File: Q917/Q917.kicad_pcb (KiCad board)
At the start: 2 copper layers, 43.2 x 17.8 mm, 6 parts, among them J1 Analog, J2 Digital

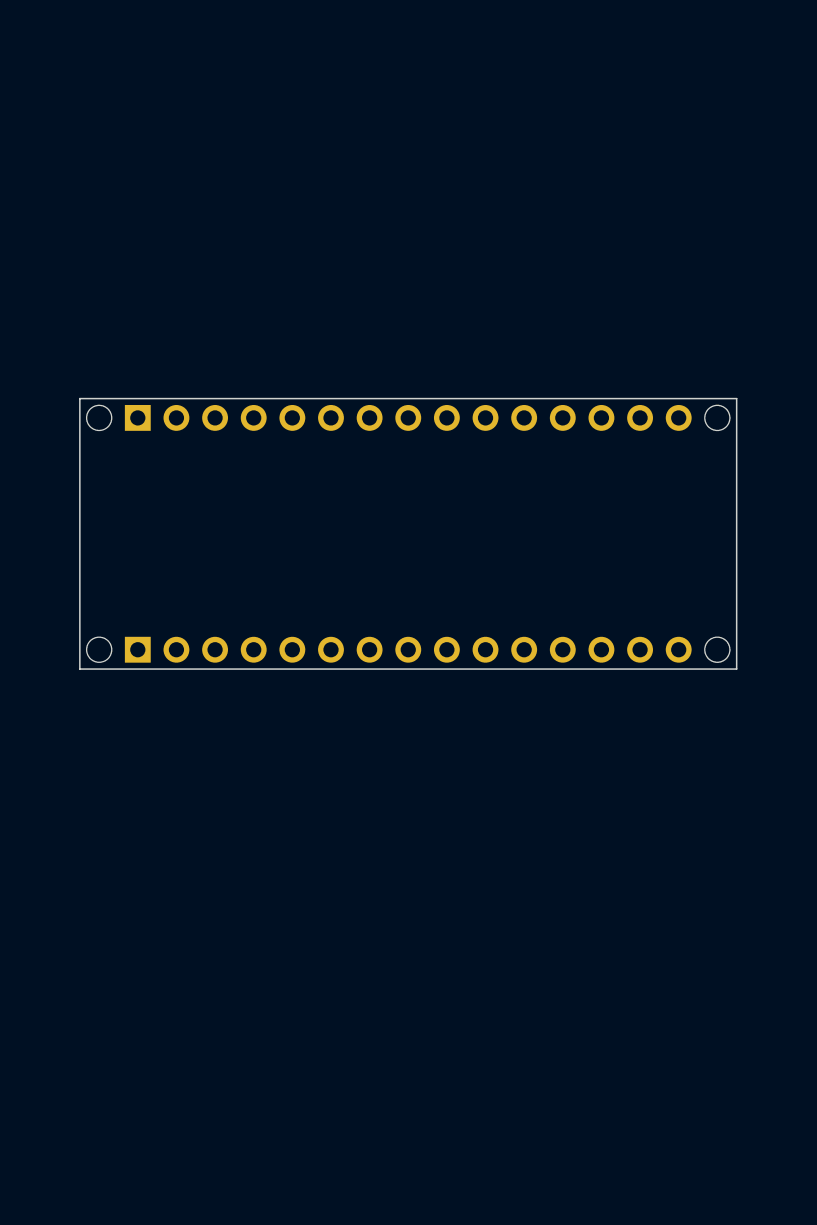
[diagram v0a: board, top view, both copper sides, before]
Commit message: sche: PCB配線開始
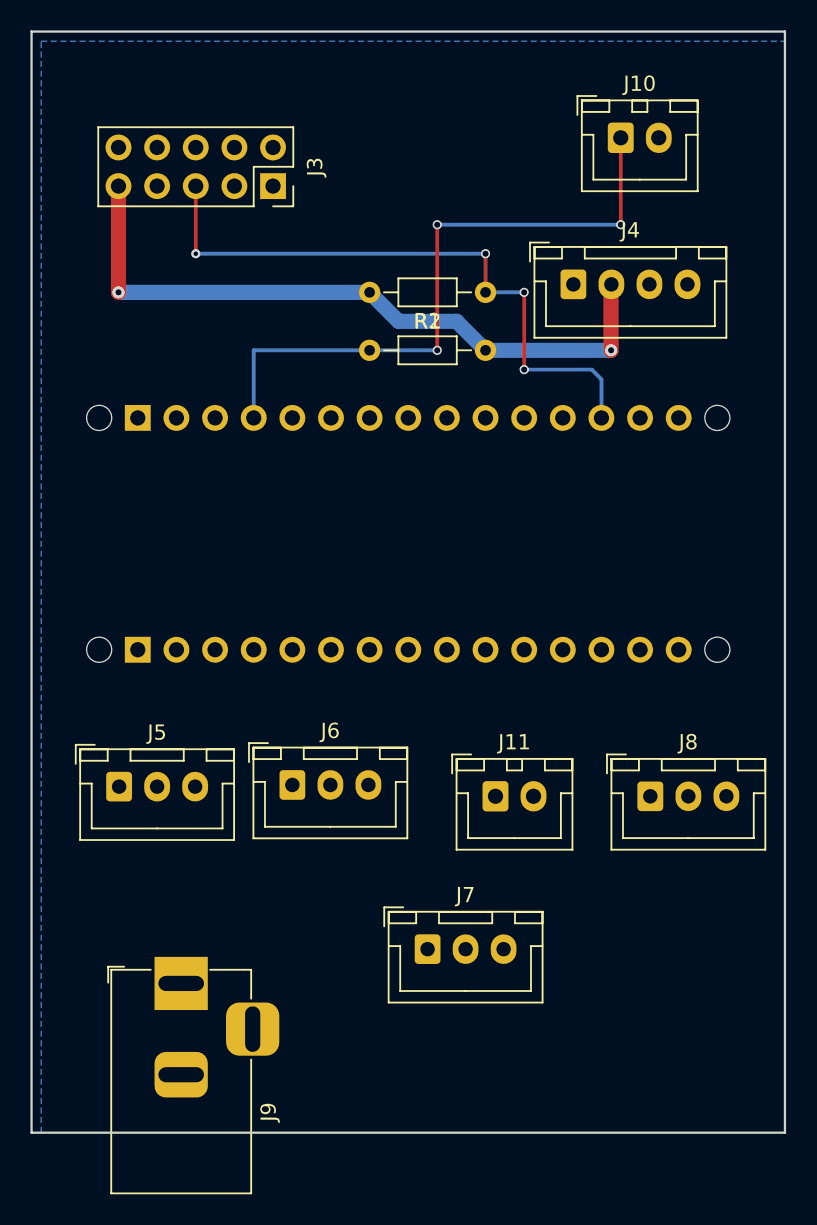
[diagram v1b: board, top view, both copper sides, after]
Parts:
- added J10: SELE, Connector_JST:JST_XH_B2B-XH-A_1x02_P2.50mm_Vertical, F.Cu at (135.6, 65.1)
- added J11: RESET, Connector_JST:JST_XH_B2B-XH-A_1x02_P2.50mm_Vertical, F.Cu at (127.3, 108.4)
- added J3: to_W5500, Connector_PinSocket_2.54mm:PinSocket_2x05_P2.54mm_Vertical, F.Cu at (112.7, 68.2)
- added J4: to_LCD, Connector_JST:JST_XH_B4B-XH-A_1x04_P2.50mm_Vertical, F.Cu at (132.4, 74.7)
- added J5: to_TEMP, Connector_JST:JST_XH_B3B-XH-A_1x03_P2.50mm_Vertical, F.Cu at (102.6, 107.7)
- added J6: to_HUMI, Connector_JST:JST_XH_B3B-XH-A_1x03_P2.50mm_Vertical, F.Cu at (114.0, 107.6)
- added J7: to_ILLU, Connector_JST:JST_XH_B3B-XH-A_1x03_P2.50mm_Vertical, F.Cu at (122.9, 118.4)
- added J8: to_ETC, Connector_JST:JST_XH_B3B-XH-A_1x03_P2.50mm_Vertical, F.Cu at (137.5, 108.4)
- added J9: DC5V, Connector_BarrelJack:BarrelJack_Horizontal, F.Cu at (106.7, 120.7)
- added R1: 10k, Resistor_THT:R_Axial_DIN0204_L3.6mm_D1.6mm_P7.62mm_Horizontal, F.Cu at (126.7, 75.2)
- added R2: 10k, Resistor_THT:R_Axial_DIN0204_L3.6mm_D1.6mm_P7.62mm_Horizontal, F.Cu at (119.0, 79.0)
- J1, J2: footprint Connector_PinHeader_2.54mm:PinHeader_1x15_P2.54mm_Vertical -> Connector_PinSocket_2.54mm:PinSocket_1x15_P2.54mm_Vertical
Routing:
- net +5V: track 0.00 -> 45.3 mm, vias 0 -> 2
- net /*D9: track 0.00 -> 42.5 mm, vias 0 -> 3
- net /~{RESET}: track 0.00 -> 41.5 mm, vias 0 -> 4
- added copper zone on B.Cu, net GND
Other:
- board size 43.2 x 17.8 mm -> 49.5 x 72.4 mm
